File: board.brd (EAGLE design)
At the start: 67.3 x 44.4 mm, 86 parts, among them J1 AVR_SPI_PRG_6NS, U1 TPS2112A, U2 MAX1555, U3 USD-SOCKETNEW, U4 3.3V, U5 2.8V, U6 74HC595, Y1 8MHz, Y2 12.288MHz

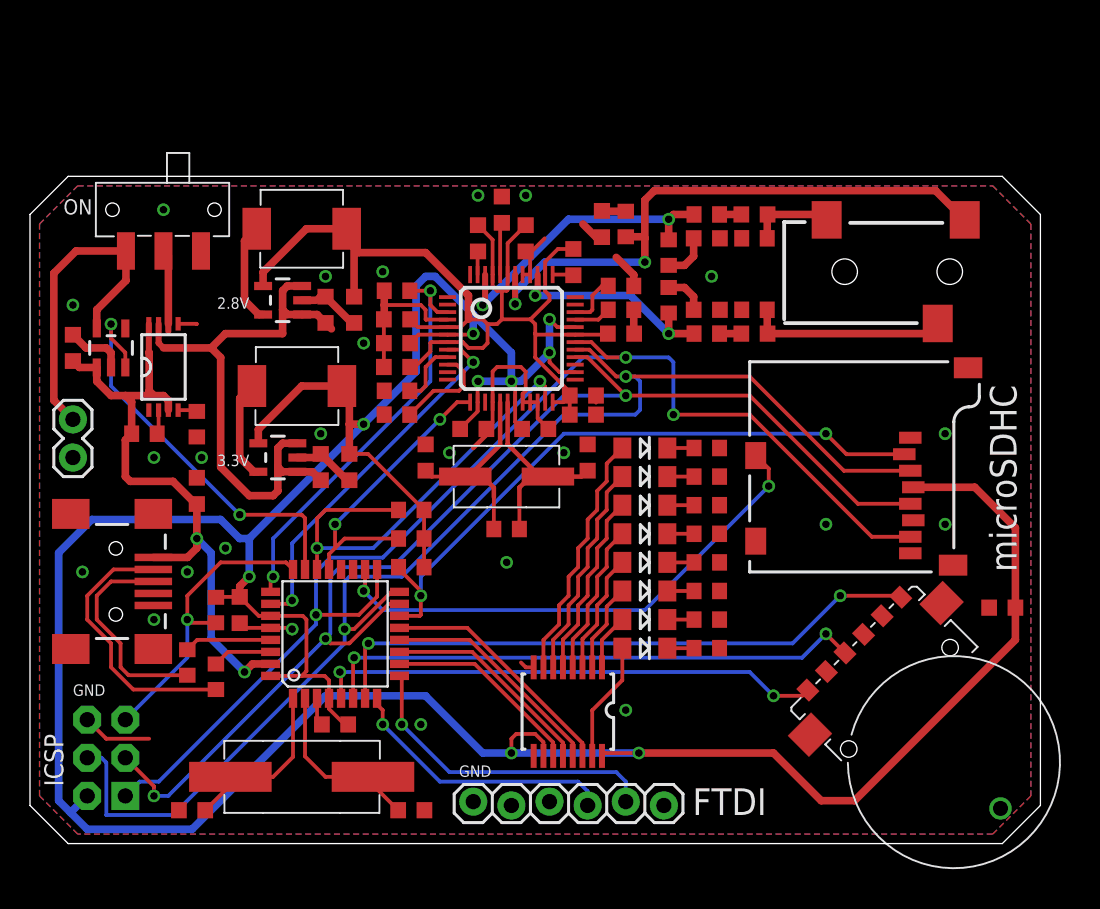
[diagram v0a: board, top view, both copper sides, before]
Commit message: Switching back to atmega32u4
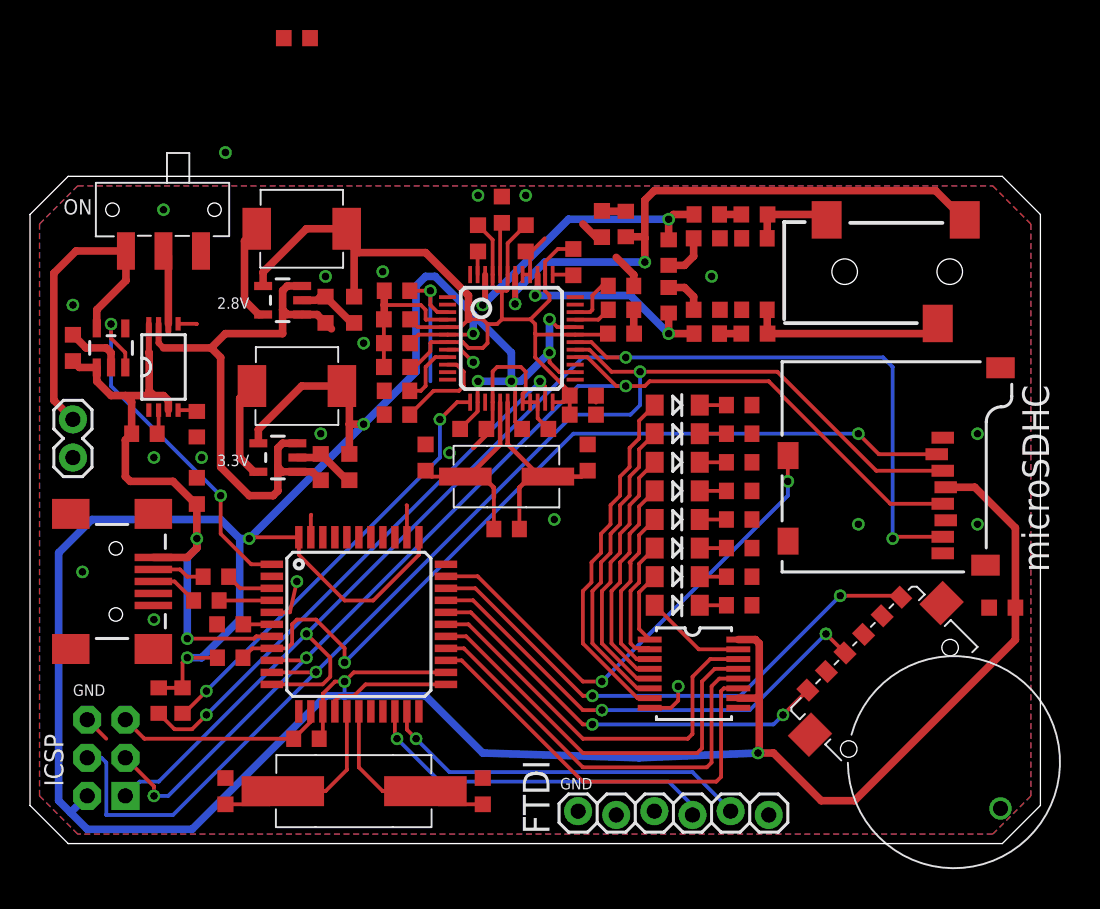
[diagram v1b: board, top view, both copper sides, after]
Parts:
- U$1: value ATMEGA32U2 -> ATMEGA32U4TQFP; device CEDT:TQFP32-08 -> SparkFun-DigitalIC:SPARKFUN-DIGITALIC_TQFP44
- moved C5 45.8 mm to (17.1, 53.0)
- moved R7 21.1 mm to (7.94, 8.89), turned to 90 degrees
- moved C3 19.4 mm to (29.5, 2.86), turned to 90 degrees
- moved R6 18.7 mm to (9.53, 8.89), turned to 90 degrees
- moved R8 13.5 mm to (12.7, 11.7), turned to 180 degrees
- moved C4 12.4 mm to (12.4, 2.86), turned to 90 degrees
- moved R5 10.5 mm to (17.8, 6.35), turned to 0 degrees
- moved U6 8.62 mm to (43.5, 10.7), turned to 270 degrees
- moved JP2 7.01 mm to (48.6, 1.27)
- moved R1 6.67 mm to (11.7, 17.1), turned to 180 degrees
- moved R2 4.32 mm to (11.1, 15.6), turned to 180 degrees
- moved Y1 3.62 mm to (21.0, 2.86), turned to 0 degrees
- moved LED3 3.58 mm to (42.5, 19.1)
- moved LED6 3.58 mm to (42.5, 24.8)
- moved LED7 3.58 mm to (42.5, 26.7)
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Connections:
- new net UCAP: C2.1, U$1.6
- net CHG_B: now also U$1.1; no longer U$1.23
- net ENCODER_A: now also U$1.31; no longer U$1.7
- net ENCODER_B: now also U$1.29; no longer U$1.5
- net ENCODER_S: now also U$1.30; no longer U$1.6
- net GND: now also U$1.15, U$1.23, U$1.35, U$1.43, U$1.5; no longer U$1.28, U$1.3
- net MISO: now also U$1.11; no longer U$1.17
- net MOSI: now also U$1.10; no longer U$1.16
- net MP3_DREQ: no longer U$1.26
- net MP3_XCS: no longer U$1.22
- net MP3_XDCS: no longer U$1.21
- net MP3_XRESET: no longer U$1.25
- net N$14: now also U$1.16; no longer U$1.2
- net N$2: now also U$1.17; no longer U$1.1
- net RESET: now also U$1.13; no longer U$1.24
- net SCK: now also U$1.9; no longer U$1.15
- net SD_CD: now also U$1.32; no longer U$1.18
- net SD_CS: now also U$1.8; no longer U$1.14
- net SERIAL_RX: now also U$1.20; no longer U$1.8
- net SERIAL_TX: now also U$1.21; no longer U$1.9
- net SHIFT_DS: now also U$1.28; no longer U$1.13
- net SHIFT_OE: now also U$1.27; no longer U$1.12
- net SHIFT_SHCP: now also U$1.25; no longer U$1.10
- net SHIFT_STCP: now also U$1.26; no longer U$1.11
- net USB_D+: now also U$1.4; no longer U$1.29
- net USB_D-: now also U$1.3; no longer U$1.30
- net VBUS: now also U$1.7; no longer U$1.31
- net VDD: now also U$1.14, U$1.24, U$1.34, U$1.44; no longer C2.1, U$1.27, U$1.32, U$1.4
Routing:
- net MP3_DREQ: track 24.5 -> 2.06 mm, vias 2 -> 1
- net MP3_XRESET: track 28.1 -> 9.70 mm, vias 2 -> 1
- net SHIFT_SHCP: track 13.3 -> 28.7 mm
- net N$1: track 18.2 -> 3.52 mm
- net SHIFT_STCP: track 14.3 -> 28.2 mm
- net SD_CS: track 43.2 -> 56.6 mm
- net VDD: track 233.3 -> 246.5 mm, vias 9 -> 10
- net SHIFT_OE: track 15.3 -> 27.6 mm
- net N$6: track 14.3 -> 3.21 mm
- net SHIFT_DS: track 16.2 -> 27.1 mm
- net GND: track 62.4 -> 71.6 mm, vias 24 -> 21
- net MP3_XDCS: track 20.0 -> 29.2 mm
- net N$19: track 16.8 -> 23.8 mm
- net MP3_XCS: track 30.1 -> 37.0 mm
- net N$20: track 14.6 -> 20.7 mm
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
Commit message: Rough connections are made.
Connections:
- net MP3_DREQ: now also U$1.38
- net MP3_XCS: now also U$1.40
- net MP3_XDCS: now also U$1.41
- net MP3_XRESET: now also U$1.39
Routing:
- net MP3_DREQ: track 2.06 -> 27.2 mm, vias 1 -> 2
- net MP3_XRESET: track 9.70 -> 29.4 mm, vias 1 -> 2
- net MP3_XCS: track 37.0 -> 50.8 mm, vias 2 -> 3
- net MOSI: track 84.8 -> 95.4 mm
- net SCK: track 77.6 -> 86.8 mm
- net MP3_XDCS: track 29.2 -> 37.2 mm, vias 2 -> 3
- net MISO: track 89.7 -> 93.8 mm
- net GND: track 71.6 -> 74.9 mm, vias 21 -> 22
- net VDD: track 246.5 -> 245.7 mm

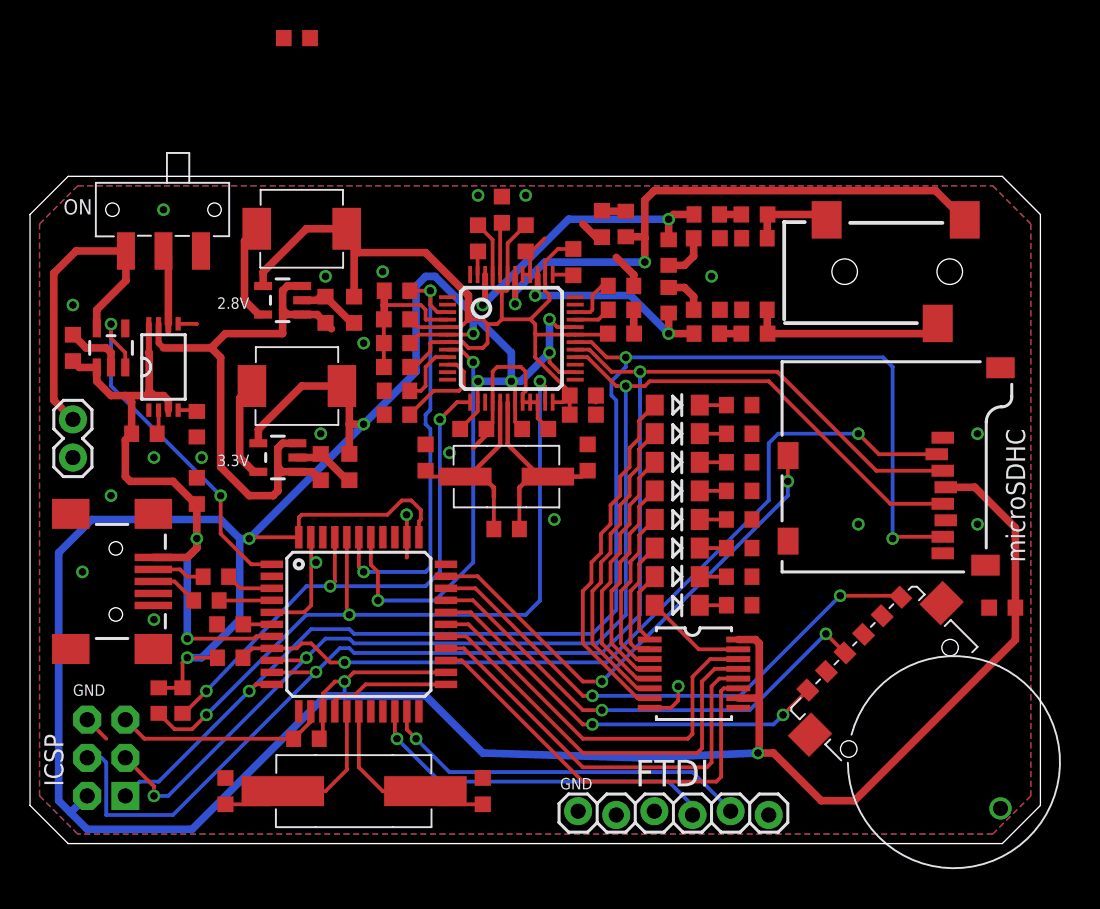
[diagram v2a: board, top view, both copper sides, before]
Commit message: More connections
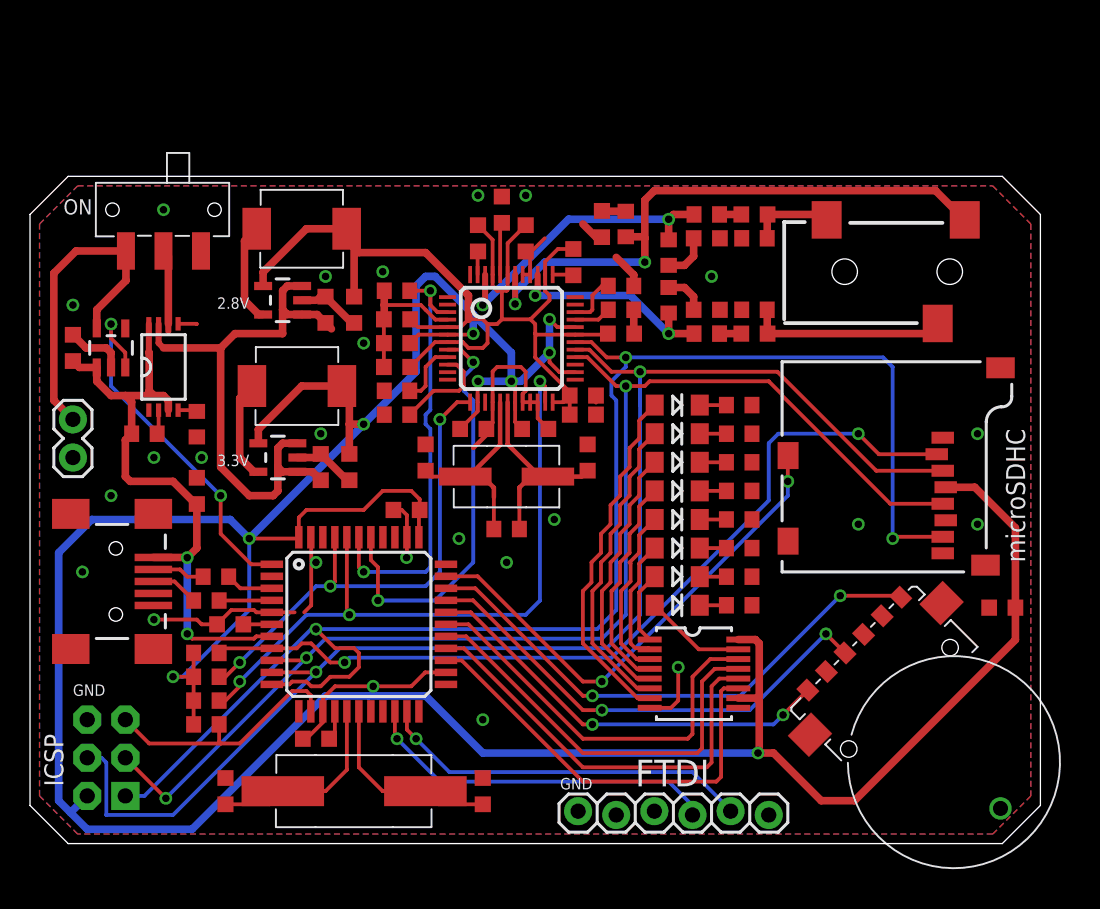
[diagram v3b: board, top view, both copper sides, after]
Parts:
- added C31: 0.1u, rcl:C0603K
- moved C5 32.3 mm to (24.4, 21.6)
- moved R5 6.74 mm to (11.1, 7.30), turned to 180 degrees
- moved R7 3.18 mm to (11.1, 8.89), turned to 180 degrees
- moved R6 2.25 mm to (11.1, 10.5), turned to 180 degrees
- moved R8 1.62 mm to (11.1, 12.1)
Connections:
- net GND: now also C31.2
- net VDD: now also C31.1
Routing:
- net MISO: track 93.8 -> 103.3 mm
- net MP3_XCS: track 50.8 -> 45.7 mm
- net MP3_XDCS: track 37.2 -> 33.6 mm
- net VDD: track 245.7 -> 248.9 mm
- net RESET: track 14.0 -> 17.0 mm
- net GND: track 74.9 -> 76.8 mm, vias 22 -> 24
- net VBUS: track 43.6 -> 41.9 mm
- net SD_CS: track 56.2 -> 57.7 mm
- net SCK: track 86.8 -> 86.0 mm
- net MP3_DREQ: track 27.2 -> 27.7 mm

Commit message: A bit more beveling on corners
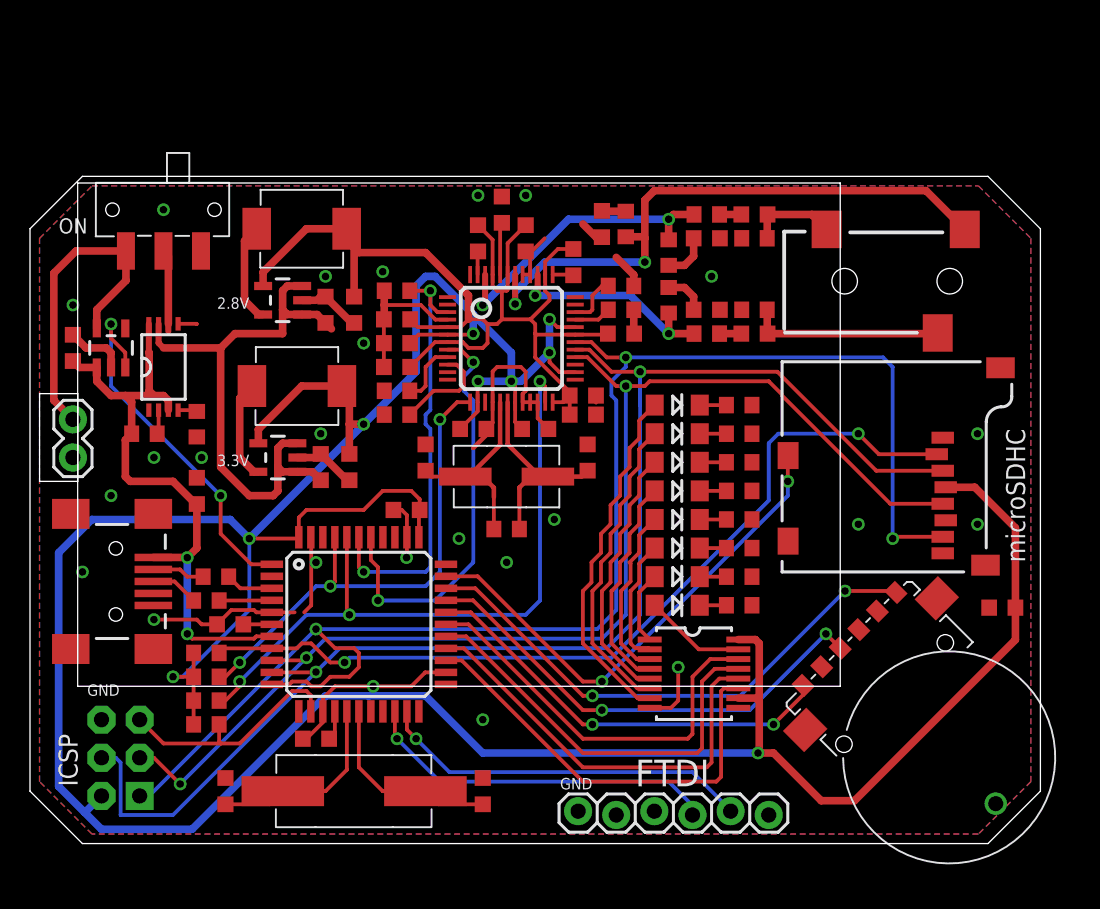
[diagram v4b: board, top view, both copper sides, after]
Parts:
- moved J1 0.95 mm to (5.40, 5.08)
- moved U7 0.64 mm to (64.1, 36.8)
- moved S2 0.45 mm to (53.3, 12.4)
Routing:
- net SCK: track 86.0 -> 84.2 mm
- net RESET: track 17.0 -> 16.0 mm
- net MOSI: track 95.2 -> 94.2 mm
- net MISO: track 103.3 -> 102.6 mm
- net VDD: track 248.9 -> 248.4 mm
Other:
- outline, holes or cut-outs redrawn

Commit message: Make wheel stick out more
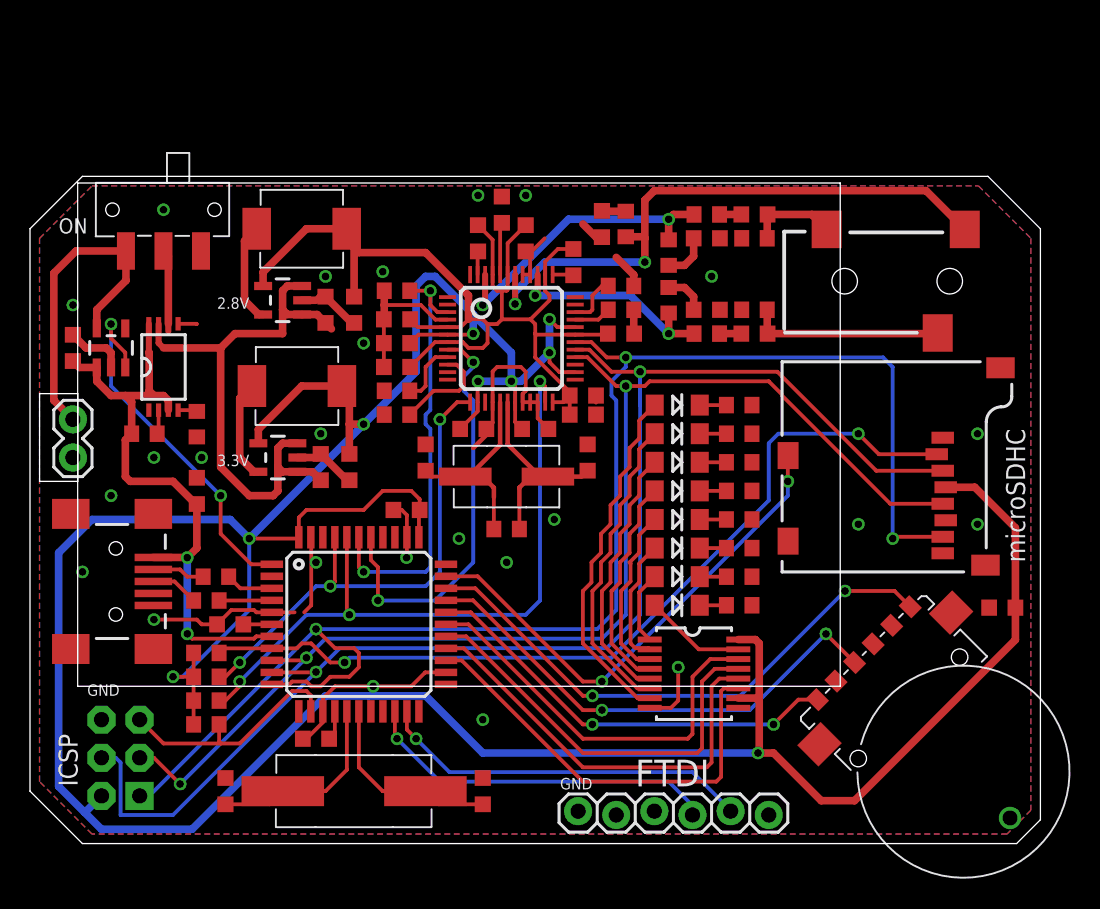
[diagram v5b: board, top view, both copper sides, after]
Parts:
- moved S2 1.35 mm to (54.3, 11.4)
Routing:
- net ENCODER_S: track 31.8 -> 33.1 mm
- net ENCODER_A: track 35.9 -> 37.2 mm
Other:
- outline, holes or cut-outs redrawn
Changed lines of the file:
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@@
 <wire x1="2.8575" y1="43.815" x2="63.1825" y2="43.815" width="0" layer="20"/>
 <wire x1="63.1825" y1="43.815" x2="66.675" y2="40.3225" width="0" layer="20"/>
-<wire x1="66.675" y1="40.3225" x2="66.675" y2="2.8575" width="0" layer="20"/>
-<wire x1="66.675" y1="2.8575" x2="63.1825" y2="-0.635" width="0" layer="20"/>
-<wire x1="63.1825" y1="-0.635" x2="2.8575" y2="-0.635" width="0" layer="20"/>
+<wire x1="66.675" y1="40.3225" x2="66.675" y2="0.9525" width="0" layer="20"/>
+<wire x1="66.675" y1="0.9525" x2="65.0875" y2="-0.635" width="0" layer="20"/>
+<wire x1="65.0875" y1="-0.635" x2="2.8575" y2="-0.635" width="0" layer="20"/>
 <wire x1="2.8575" y1="-0.635" x2="-0.635" y2="2.8575" width="0" layer="20"/>
 <text x="62.23" y="0.635" size="1.778" layer="22" rot="MR0">MJK
@@
 </element>
 <element name="C6" library="rcl" package="C0603K" value="1u" x="2.2225" y="32.385" smashed="yes" rot="R90"/>
-<element name="S2" library="mkmp3" package="EVQ-WKA" value="EVQ-WKA" x="53.34" y="12.3825" smashed="yes" rot="R225"/>
+<element name="S2" library="mkmp3" package="EVQ-WKA" value="EVQ-WKA" x="54.2925" y="11.43" smashed="yes" rot="R225"/>
 <element name="U7" library="mkmp3" package="AUDIO-JACK-3.5MM-SMD" value="" x="64.135" y="36.83" smashed="yes" rot="R180"/>
 <element name="LED8" library="LilyPad-Wearables" package="LED-1206" value="" x="42.4815" y="28.575" smashed="yes">
@@
 <vertex x="62.5475" y="43.18"/>
 <vertex x="66.04" y="39.6875"/>
-<vertex x="66.04" y="3.4925"/>
-<vertex x="62.5475" y="0"/>
+<vertex x="66.04" y="1.5875"/>
+<vertex x="64.4525" y="0"/>
 </polygon>
 <polygon width="0.508" layer="1" isolate="0.4064">
@@
 <vertex x="62.5475" y="43.18"/>
 <vertex x="66.04" y="39.6875"/>
-<vertex x="66.04" y="3.4925"/>
-<vertex x="62.5475" y="0"/>
+<vertex x="66.04" y="1.5875"/>
+<vertex x="64.4525" y="0"/>
 </polygon>
 <contactref element="C2" pad="2"/>
@@
 <via x="53.6575" y="16.1925" extent="1-16" drill="0.5"/>
 <wire x1="53.6575" y1="16.1925" x2="56.95461875" y2="16.1925" width="0.254" layer="1"/>
-<wire x1="56.95461875" y1="16.1925" x2="57.052309375" y2="16.094809375" width="0.254" layer="1"/>
+<wire x1="56.95461875" y1="16.1925" x2="58.004809375" y2="15.142309375" width="0.254" layer="1"/>
 <contactref element="U$1" pad="31"/>
 <wire x1="53.6575" y1="16.1925" x2="46.6725" y2="9.2075" width="0.254" layer="16"/>
@@
 <wire x1="36.83" y1="7.3025" x2="48.895" y2="7.3025" width="0.254" layer="16"/>
 <via x="48.895" y="7.3025" extent="1-16" drill="0.5"/>
-<wire x1="48.895" y1="7.3025" x2="50.865125" y2="9.272625" width="0.254" layer="1"/>
-<wire x1="50.865125" y1="9.272625" x2="50.865125" y2="9.907625" width="0.254" layer="1"/>
+<wire x1="51.817625" y1="8.955125" x2="50.547625" y2="8.955125" width="0.254" layer="1"/>
+<wire x1="50.547625" y1="8.955125" x2="48.895" y2="7.3025" width="0.254" layer="1"/>
 </signal>
 <signal name="ENCODER_S">
 <contactref element="S2" pad="4"/>
 <via x="52.3875" y="13.335" extent="1-16" drill="0.5"/>
-<wire x1="52.3875" y1="13.335" x2="53.34" y2="12.3825" width="0.254" layer="1"/>
+<wire x1="52.3875" y1="13.335" x2="54.2925" y2="11.43" width="0.254" layer="1"/>
 <contactref element="U$1" pad="30"/>
 <wire x1="52.3875" y1="13.335" x2="47.3075" y2="8.255" width="0.254" layer="16"/>
